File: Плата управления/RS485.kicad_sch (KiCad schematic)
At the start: 0 parts

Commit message: Добавил разъёмы под интерфейсы
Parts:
- added C18: 0.1u, Capacitor_SMD:C_0603_1608Metric_Pad1.08x0.95mm_HandSolder, symbol Device:C_Small
- added R30: 120, Resistor_SMD:R_0603_1608Metric_Pad0.98x0.95mm_HandSolder, symbol Device:R_Small
- added U6: ADM3491ExR, Package_SO:SOIC-14_3.9x8.7mm_P1.27mm, symbol Interface_UART:ADM3491ExR
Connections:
- new net +3.3V: C18.2, U6.13 (VCC), U6.14 (VCC)
- new net GND: C18.1, U6.6 (GND), U6.7 (GND)
- new net RS_485_A: R30.2, U6.12 (A)
- new net RS_485_B: R30.1, U6.11 (B)
- new net RS_485_Enable_MCU: U6.3 (~{RE}), U6.4 (DE)
- new net RS_485_Y: U6.9 (Y)
- new net RS_485_Z: U6.10 (Z)
- new net RX_MCU: U6.2 (RO)
- new net TX_MCU: U6.5 (DI)

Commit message: Редактировал схему
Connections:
- net RX_MCU renamed RS_485_RX_MCU
- net TX_MCU renamed RS_485_TX_MCU
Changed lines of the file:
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@@
     )
   )
-  (global_label "RX_MCU" (shape output) (at 82.55 57.15 180) (fields_autoplaced)
+  (global_label "RS_485_RX_MCU" (shape output) (at 82.55 57.15 180) (fields_autoplaced)
     (effects (font (size 1.27 1.27)) (justify right))
-    (property "Intersheetrefs" "${INTERSHEET_REFS}" (at 72.1452 57.15 0)
+    (property "Intersheetrefs" "${INTERSHEET_REFS}" (at 64.0226 57.15 0)
       (effects (font (size 1.27 1.27)) (justify right) hide)
     )
@@
     )
   )
-  (global_label "TX_MCU" (shape input) (at 82.55 67.31 180) (fields_autoplaced)
+  (global_label "RS_485_TX_MCU" (shape input) (at 82.55 67.31 180) (fields_autoplaced)
     (effects (font (size 1.27 1.27)) (justify right))
-    (property "Intersheetrefs" "${INTERSHEET_REFS}" (at 72.4476 67.31 0)
+    (property "Intersheetrefs" "${INTERSHEET_REFS}" (at 64.325 67.31 0)
       (effects (font (size 1.27 1.27)) (justify right) hide)
     )

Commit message: Собираю документацию
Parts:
- added D9: PSM712-LF-T7, Package_TO_SOT_SMD:SOT-23, symbol Power_Protection:NUP2105L
- U6: value ADM3491ExR -> ADM3491ARZ
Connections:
- net GND: now also D9.3 (A)
- net RS_485_A: now also D9.1 (K)
- net RS_485_B: now also D9.2 (K)
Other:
- moved on the sheet: R30
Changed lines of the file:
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@@
   (junction (at 81.28 60.96) (diameter 0) (color 0 0 0 0)
   )
-  (junction (at 104.14 59.69) (diameter 0) (color 0 0 0 0)
-  )
-  (junction (at 104.14 54.61) (diameter 0) (color 0 0 0 0)
+  (junction (at 107.95 59.69) (diameter 0) (color 0 0 0 0)
+  )
+  (junction (at 107.95 54.61) (diameter 0) (color 0 0 0 0)
   )
   (wire (pts (xy 92.71 44.45) (xy 92.71 46.99))
     (stroke (width 0) (type default))
   )
-  (wire (pts (xy 102.87 59.69) (xy 104.14 59.69))
+  (wire (pts (xy 102.87 59.69) (xy 107.95 59.69))
     (stroke (width 0) (type default))
   )
@@
     (stroke (width 0) (type default))
   )
-  (wire (pts (xy 102.87 54.61) (xy 104.14 54.61))
+  (wire (pts (xy 107.95 62.23) (xy 107.95 59.69))
+    (stroke (width 0) (type default))
+  )
+  (wire (pts (xy 135.89 52.07) (xy 107.95 52.07))
     (stroke (width 0) (type default))
   )
@@
     (stroke (width 0) (type default))
   )
+  (wire (pts (xy 107.95 52.07) (xy 107.95 54.61))
+    (stroke (width 0) (type default))
+  )
   (wire (pts (xy 77.47 44.45) (xy 82.55 44.45))
     (stroke (width 0) (type default))
@@
     (stroke (width 0) (type default))
   )
-  (wire (pts (xy 104.14 54.61) (xy 111.76 54.61))
-    (stroke (width 0) (type default))
-  )
   (wire (pts (xy 81.28 59.69) (xy 81.28 60.96))
     (stroke (width 0) (type default))
   )
+  (wire (pts (xy 134.62 59.69) (xy 135.89 59.69))
+    (stroke (width 0) (type default))
+  )
   (wire (pts (xy 87.63 44.45) (xy 92.71 44.45))
     (stroke (width 0) (type default))
   )
+  (wire (pts (xy 135.89 59.69) (xy 135.89 62.23))
+    (stroke (width 0) (type default))
+  )
+  (wire (pts (xy 135.89 54.61) (xy 135.89 52.07))
+    (stroke (width 0) (type default))
+  )
+  (wire (pts (xy 102.87 54.61) (xy 107.95 54.61))
+    (stroke (width 0) (type default))
+  )
   (wire (pts (xy 77.47 43.18) (xy 77.47 44.45))
     (stroke (width 0) (type default))
@@
     (stroke (width 0) (type default))
   )
-  (wire (pts (xy 104.14 59.69) (xy 111.76 59.69))
-    (stroke (width 0) (type default))
-  )
   (wire (pts (xy 81.28 60.96) (xy 81.28 62.23))
     (stroke (width 0) (type default))
   )
+  (wire (pts (xy 134.62 54.61) (xy 135.89 54.61))
+    (stroke (width 0) (type default))
+  )
   (wire (pts (xy 78.74 60.96) (xy 81.28 60.96))
+    (stroke (width 0) (type default))
+  )
+  (wire (pts (xy 135.89 62.23) (xy 107.95 62.23))
     (stroke (width 0) (type default))
   )
@@
     )
   )
-  (global_label "RS_485_A" (shape input) (at 111.76 54.61 0) (fields_autoplaced)
+  (global_label "RS_485_A" (shape input) (at 135.89 54.61 0) (fields_autoplaced)
     (effects (font (size 1.27 1.27)) (justify left))
-    (property "Intersheetrefs" "${INTERSHEET_REFS}" (at 123.7976 54.61 0)
+    (property "Intersheetrefs" "${INTERSHEET_REFS}" (at 147.9276 54.61 0)
       (effects (font (size 1.27 1.27)) (justify left) hide)
     )
@@
     )
   )
-  (global_label "RS_485_B" (shape input) (at 111.76 59.69 0) (fields_autoplaced)
+  (global_label "RS_485_B" (shape input) (at 135.89 59.69 0) (fields_autoplaced)
     (effects (font (size 1.27 1.27)) (justify left))
-    (property "Intersheetrefs" "${INTERSHEET_REFS}" (at 123.979 59.69 0)
+    (property "Intersheetrefs" "${INTERSHEET_REFS}" (at 148.109 59.69 0)
       (effects (font (size 1.27 1.27)) (justify left) hide)
     )
@@
   (symbol (lib_id "Interface_UART:ADM3491ExR") (at 92.71 62.23 0) (unit 1)
     (in_bom yes) (on_board yes) (dnp no) (fields_autoplaced)
-    (property "Reference" "U6" (at 94.6659 45.72 0)
+    (property "Reference" "U6" (at 94.9041 44.45 0)
       (effects (font (size 1.27 1.27)) (justify left))
     )
-    (property "Value" "ADM3491ExR" (at 94.6659 48.26 0)
+    (property "Value" "ADM3491ARZ" (at 94.9041 46.99 0)
       (effects (font (size 1.27 1.27)) (justify left))
     )
@@
     )
   )
-  (symbol (lib_id "Device:R_Small") (at 104.14 57.15 180) (unit 1)
+  (symbol (lib_id "Device:R_Small") (at 107.95 57.15 180) (unit 1)
     (in_bom yes) (on_board yes) (dnp no)
-    (property "Reference" "R30" (at 106.68 55.88 0)
+    (property "Reference" "R30" (at 110.49 55.88 0)
       (effects (font (size 1.27 1.27)) (justify right))
     )
-    (property "Value" "120" (at 106.68 58.42 0)
+    (property "Value" "120" (at 110.49 58.42 0)
       (effects (font (size 1.27 1.27)) (justify right))
     )
-    (property "Footprint" "Resistor_SMD:R_0603_1608Metric_Pad0.98x0.95mm_HandSolder" (at 104.14 57.15 0)
-      (effects (font (size 1.27 1.27)) hide)
-    )
-    (property "Datasheet" "~" (at 104.14 57.15 0)
+    (property "Footprint" "Resistor_SMD:R_0603_1608Metric_Pad0.98x0.95mm_HandSolder" (at 107.95 57.15 0)
+      (effects (font (size 1.27 1.27)) hide)
+    )
+    (property "Datasheet" "~" (at 107.95 57.15 0)
       (effects (font (size 1.27 1.27)) hide)
     )
@@
     )
   )
+  (symbol (lib_id "Power_Protection:NUP2105L") (at 129.54 57.15 270) (unit 1)
+    (in_bom yes) (on_board yes) (dnp no) (fields_autoplaced)
+    (property "Reference" "D9" (at 129.54 48.26 90)
+      (effects (font (size 1.27 1.27)))
+    )
+    (property "Value" "PSM712-LF-T7" (at 129.54 50.8 90)
+      (effects (font (size 1.27 1.27)))
+    )
+    (property "Footprint" "Package_TO_SOT_SMD:SOT-23" (at 128.27 62.865 0)
+      (effects (font (size 1.27 1.27)) (justify left) hide)
+    )
+    (property "Datasheet" "http://www.onsemi.com/pub_link/Collateral/NUP2105L-D.PDF" (at 132.715 60.325 0)
+      (effects (font (size 1.27 1.27)) hide)
+    )
+    (pin "3")
+    (pin "1")
+    (pin "2")
+    (instances
+      (project "Плата управления"
+        (path "/75f4c67c-bbde-4446-8f82-67797a1b269f/9fed4cc9-7de2-4454-9cda-928fae308673"
+          (reference "D9") (unit 1)
+        )
+        (path "/75f4c67c-bbde-4446-8f82-67797a1b269f/c4a77b60-6f80-4c82-a865-c1484ac69908"
+          (reference "D11") (unit 1)
+        )
+      )
+    )
+  )
   (symbol (lib_id "power:+3.3V") (at 92.71 43.18 0) (unit 1)
     (in_bom yes) (on_board yes) (dnp no) (fields_autoplaced)
@@
         )
       )
+    )
+  )
+  (symbol (lib_id "power:GND") (at 124.46 57.15 270) (unit 1)
+    (in_bom yes) (on_board yes) (dnp no) (fields_autoplaced)
+    (property "Reference" "#PWR074" (at 118.11 57.15 0)
+      (effects (font (size 1.27 1.27)) hide)
+    )
+    (property "Value" "GND" (at 120.65 57.15 90)
+      (effects (font (size 1.27 1.27)) (justify right))
+    )
+    (property "Footprint" "" (at 124.46 57.15 0)
+      (effects (font (size 1.27 1.27)) hide)
+    )
+    (property "Datasheet" "" (at 124.46 57.15 0)
+      (effects (font (size 1.27 1.27)) hide)
+    )
+    (pin "1")
+    (instances
+      (project "Плата управления"
+        (path "/75f4c67c-bbde-4446-8f82-67797a1b269f/c4a77b60-6f80-4c82-a865-c1484ac69908"
+          (reference "#PWR074") (unit 1)
+        )
+      )

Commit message: Добавил документы
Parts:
- R30: footprint Resistor_SMD:R_0603_1608Metric_Pad0.98x0.95mm_HandSolder -> Resistor_SMD:R_0805_2012Metric
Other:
- note added: "RS-485"
- moved on the sheet: C18, D9, R30, U6

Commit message: Добавил все документы
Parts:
- renumbered U6 to U8
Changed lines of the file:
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@@
   (symbol (lib_id "Interface_UART:ADM3491ExR") (at 149.86 99.06 0) (unit 1)
     (in_bom yes) (on_board yes) (dnp no)
-    (property "Reference" "U6" (at 142.24 85.09 0)
+    (property "Reference" "U8" (at 142.24 85.09 0)
       (effects (font (size 1.27 1.27)) (justify left))
     )
@@
       (project "Плата управления"
         (path "/75f4c67c-bbde-4446-8f82-67797a1b269f/c4a77b60-6f80-4c82-a865-c1484ac69908"
-          (reference "U6") (unit 1)
+          (reference "U8") (unit 1)
         )
       )
@@
         )
         (path "/75f4c67c-bbde-4446-8f82-67797a1b269f/c4a77b60-6f80-4c82-a865-c1484ac69908"
-          (reference "C59") (unit 1)
+          (reference "C32") (unit 1)
         )
       )
@@
         )
         (path "/75f4c67c-bbde-4446-8f82-67797a1b269f/c4a77b60-6f80-4c82-a865-c1484ac69908"
-          (reference "R38") (unit 1)
+          (reference "R31") (unit 1)
         )
       )
@@
         )
         (path "/75f4c67c-bbde-4446-8f82-67797a1b269f/c4a77b60-6f80-4c82-a865-c1484ac69908"
-          (reference "D11") (unit 1)
+          (reference "D6") (unit 1)
         )
       )
@@
   (symbol (lib_id "power:+3.3V") (at 149.86 80.01 0) (unit 1)
     (in_bom yes) (on_board yes) (dnp no) (fields_autoplaced)
-    (property "Reference" "#PWR0124" (at 149.86 83.82 0)
+    (property "Reference" "#PWR072" (at 149.86 83.82 0)
       (effects (font (size 1.27 1.27)) hide)
     )
@@
       (project "Плата управления"
         (path "/75f4c67c-bbde-4446-8f82-67797a1b269f/c4a77b60-6f80-4c82-a865-c1484ac69908"
-          (reference "#PWR0124") (unit 1)
+          (reference "#PWR072") (unit 1)
         )
       )
@@
   (symbol (lib_id "power:GND") (at 134.62 80.01 180) (unit 1)
     (in_bom yes) (on_board yes) (dnp no) (fields_autoplaced)
-    (property "Reference" "#PWR0125" (at 134.62 73.66 0)
+    (property "Reference" "#PWR071" (at 134.62 73.66 0)
       (effects (font (size 1.27 1.27)) hide)
     )
@@
       (project "Плата управления"
         (path "/75f4c67c-bbde-4446-8f82-67797a1b269f/c4a77b60-6f80-4c82-a865-c1484ac69908"
-          (reference "#PWR0125") (unit 1)
+          (reference "#PWR071") (unit 1)
         )
       )
@@
   (symbol (lib_id "power:GND") (at 149.86 114.3 0) (unit 1)
     (in_bom yes) (on_board yes) (dnp no) (fields_autoplaced)
-    (property "Reference" "#PWR0123" (at 149.86 120.65 0)
+    (property "Reference" "#PWR074" (at 149.86 120.65 0)
       (effects (font (size 1.27 1.27)) hide)
     )
@@
       (project "Плата управления"
         (path "/75f4c67c-bbde-4446-8f82-67797a1b269f/c4a77b60-6f80-4c82-a865-c1484ac69908"
-          (reference "#PWR0123") (unit 1)
+          (reference "#PWR074") (unit 1)
         )
       )
@@
   (symbol (lib_id "power:GND") (at 181.61 93.98 270) (unit 1)
     (in_bom yes) (on_board yes) (dnp no) (fields_autoplaced)
-    (property "Reference" "#PWR074" (at 175.26 93.98 0)
+    (property "Reference" "#PWR073" (at 175.26 93.98 0)
       (effects (font (size 1.27 1.27)) hide)
     )
@@
       (project "Плата управления"
         (path "/75f4c67c-bbde-4446-8f82-67797a1b269f/c4a77b60-6f80-4c82-a865-c1484ac69908"
-          (reference "#PWR074") (unit 1)
-        )
-      )
+          (reference "#PWR073") (unit 1)
+        )
+      )

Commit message: Версия под отчёт
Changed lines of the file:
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@@
   )
   (text "RS-485" (at 153.67 64.77 0)
-    (effects (font (size 2 2) (thickness 0.4) bold) (justify left bottom))
+    (effects (font (size 2.5 2.5) (thickness 0.4) bold) (justify left bottom))
   )
   (global_label "RS_485_Enable_MCU" (shape input) (at 135.89 97.79 180) (fields_autoplaced)

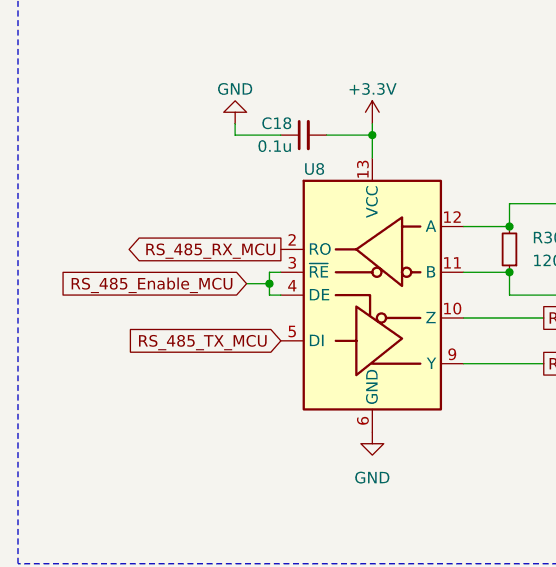
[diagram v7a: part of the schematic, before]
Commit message: Исправил RX и TX у шины RS485 и разъединил ножки управления шиной
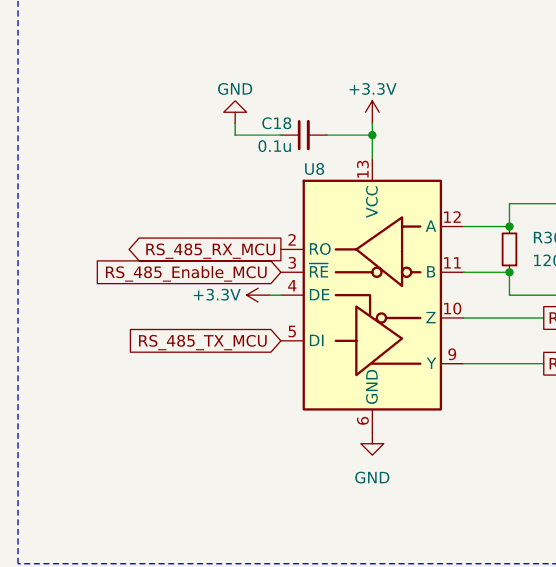
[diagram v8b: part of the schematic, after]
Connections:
- net +3.3V: now also U8.4 (DE)
- net RS_485_Enable_MCU: no longer U8.4 (DE)
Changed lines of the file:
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@@
   (junction (at 149.86 81.28) (diameter 0) (color 0 0 0 0)
   )
-  (junction (at 138.43 97.79) (diameter 0) (color 0 0 0 0)
-  )
   (junction (at 165.1 96.52) (diameter 0) (color 0 0 0 0)
   )
@@
     (stroke (width 0) (type default))
   )
-  (wire (pts (xy 139.7 96.52) (xy 138.43 96.52))
-    (stroke (width 0) (type default))
-  )
   (wire (pts (xy 138.43 99.06) (xy 139.7 99.06))
     (stroke (width 0) (type default))
@@
     (stroke (width 0) (type default))
   )
-  (wire (pts (xy 138.43 96.52) (xy 138.43 97.79))
-    (stroke (width 0) (type default))
-  )
   (wire (pts (xy 191.77 96.52) (xy 193.04 96.52))
     (stroke (width 0) (type default))
@@
     (stroke (width 0) (type default))
   )
-  (wire (pts (xy 138.43 97.79) (xy 138.43 99.06))
-    (stroke (width 0) (type default))
-  )
   (wire (pts (xy 191.77 91.44) (xy 193.04 91.44))
-    (stroke (width 0) (type default))
-  )
-  (wire (pts (xy 135.89 97.79) (xy 138.43 97.79))
     (stroke (width 0) (type default))
   )
@@
     (effects (font (size 2.5 2.5) (thickness 0.4) bold) (justify left bottom))
   )
-  (global_label "RS_485_Enable_MCU" (shape input) (at 135.89 97.79 180) (fields_autoplaced)
+  (global_label "RS_485_Enable_MCU" (shape input) (at 139.7 96.52 180) (fields_autoplaced)
     (effects (font (size 1.27 1.27)) (justify right))
-    (property "Intersheetrefs" "${INTERSHEET_REFS}" (at 113.5717 97.79 0)
+    (property "Intersheetrefs" "${INTERSHEET_REFS}" (at 117.3817 96.52 0)
       (effects (font (size 1.27 1.27)) (justify right) hide)
     )
@@
         )
       )
+    )
+  )
+  (symbol (lib_id "power:+3.3V") (at 138.43 99.06 90) (unit 1)
+    (in_bom yes) (on_board yes) (dnp no) (fields_autoplaced)
+    (property "Reference" "#PWR0110" (at 142.24 99.06 0)
+      (effects (font (size 1.27 1.27)) hide)
+    )
+    (property "Value" "+3.3V" (at 135.255 99.06 90)
+      (effects (font (size 1.27 1.27)) (justify left))
+    )
+    (property "Footprint" "" (at 138.43 99.06 0)
+      (effects (font (size 1.27 1.27)) hide)
+    )
+    (property "Datasheet" "" (at 138.43 99.06 0)
+      (effects (font (size 1.27 1.27)) hide)
+    )
+    (pin "1")
+    (instances
+      (project "Плата управления"
+        (path "/75f4c67c-bbde-4446-8f82-67797a1b269f/c4a77b60-6f80-4c82-a865-c1484ac69908"
+          (reference "#PWR0110") (unit 1)
+        )
+      )
